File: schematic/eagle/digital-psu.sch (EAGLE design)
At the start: 79 parts, among them IC1 TL072P, IC2 TLC272P, Q1 MPSA56-TO92, T3 2N3055, T4 2N3055, T5 2N3055, X1 Vout, X2 PASS_TRANSISTORS, X3 AC_IN

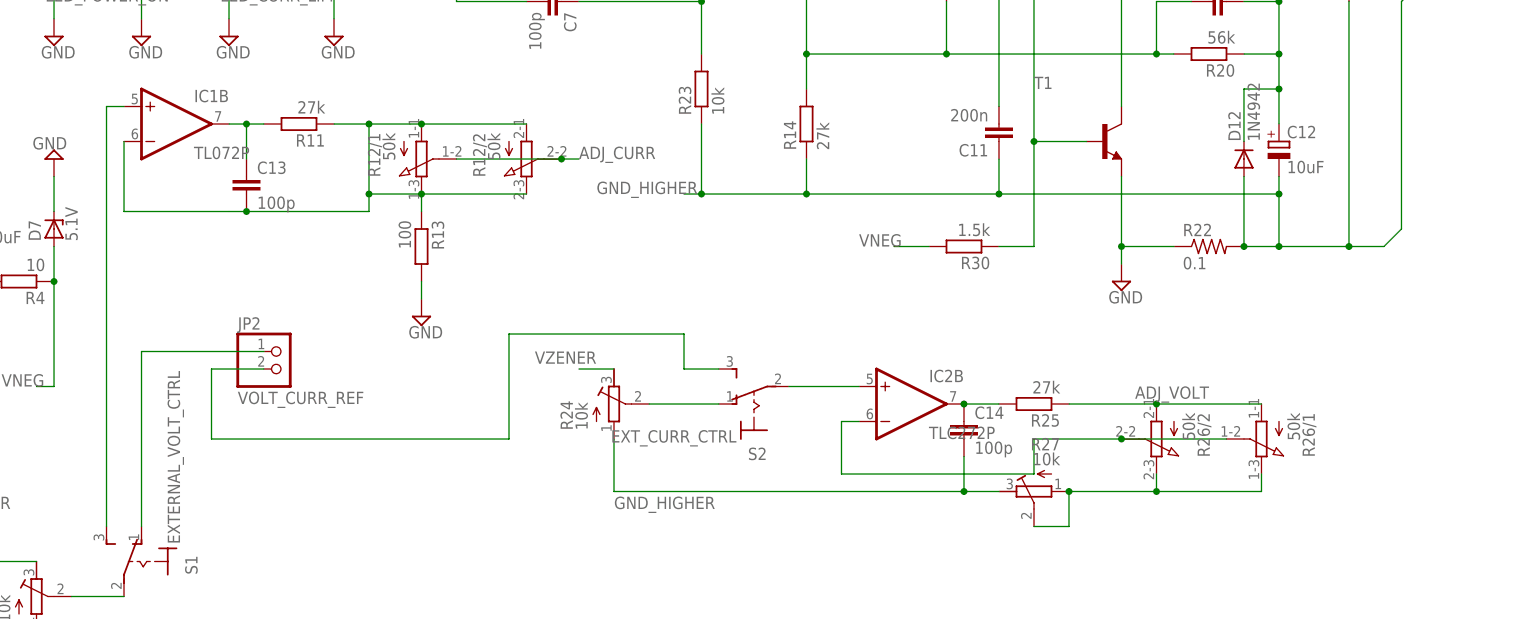
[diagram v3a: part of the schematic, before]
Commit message: op amp 27k protection fixed
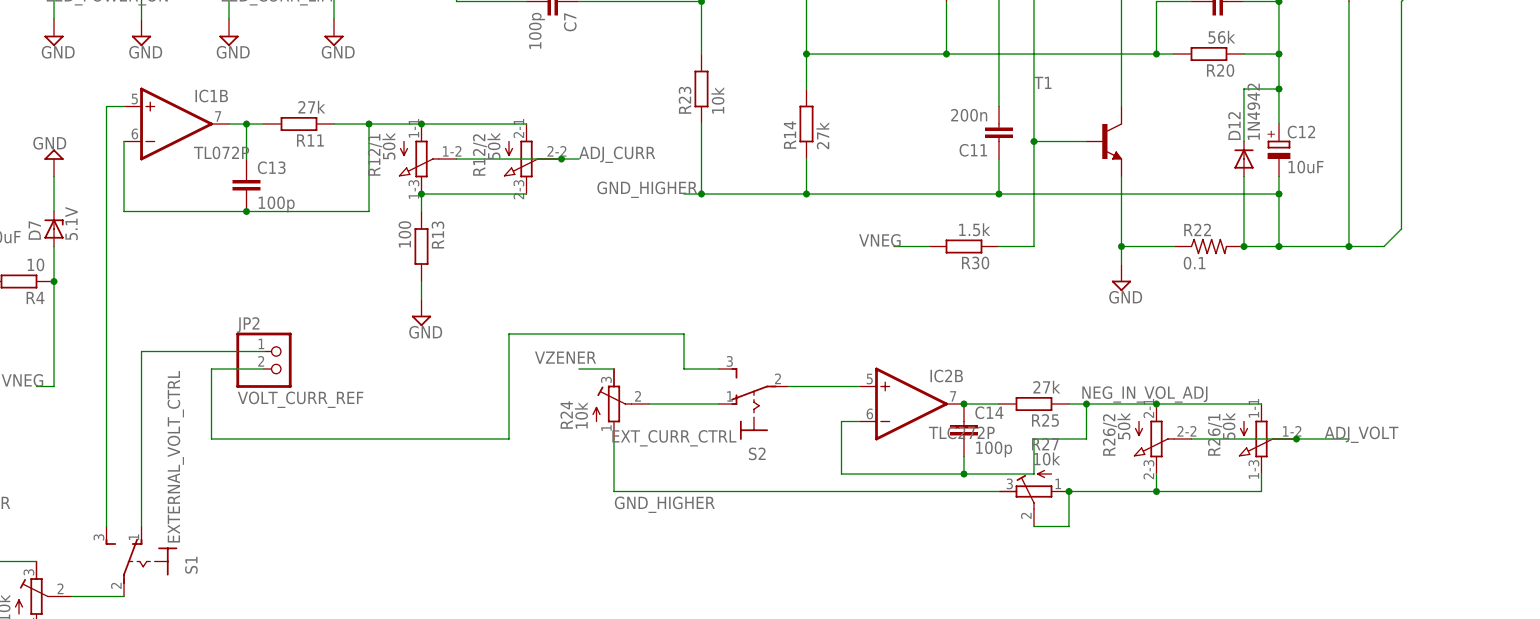
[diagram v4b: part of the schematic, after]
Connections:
- new net NEG_IN_VOL_ADJ: C14.2, IC2B.-IN, R25.1, R26/1.A, R26/2.A
- net ADJ_VOLT: now also R26/1.S, R26/2.S; no longer R25.1, R26/1.A, R26/2.A
- net GND_HIGHER: no longer C14.2
- net N$2: now also R12/1.E, R12/2.E, R13.1; no longer IC2B.-IN, R26/1.S, R26/2.S
- net N$20: no longer R12/1.E, R12/2.E, R13.1
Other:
- moved on the sheet: R26/1, R26/2
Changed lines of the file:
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@@
 <instance part="R17" gate="G$1" x="325.12" y="309.88"/>
 <instance part="R18" gate="G$1" x="320.04" y="299.72"/>
-<instance part="R26" gate="/1" x="320.04" y="208.28" rot="R180"/>
-<instance part="R26" gate="/2" x="304.8" y="208.28" rot="R180"/>
+<instance part="R26" gate="/1" x="320.04" y="208.28" rot="MR180"/>
+<instance part="R26" gate="/2" x="304.8" y="208.28" rot="MR180"/>
 <instance part="S1" gate="1" x="157.48" y="190.5" rot="MR0"/>
 <instance part="S2" gate="1" x="246.38" y="213.36" rot="R90"/>
@@
 <pinref part="R11" gate="G$1" pin="1"/>
 <wire x1="172.72" y1="241.3" x2="190.5" y2="241.3" width="0.1524" layer="91"/>
-<wire x1="190.5" y1="243.84" x2="190.5" y2="254" width="0.1524" layer="91"/>
+<wire x1="190.5" y1="241.3" x2="190.5" y2="254" width="0.1524" layer="91"/>
 <wire x1="190.5" y1="254" x2="185.42" y2="254" width="0.1524" layer="91"/>
 <pinref part="C13" gate="G$1" pin="2"/>
@@
 <junction x="198.12" y="254"/>
 <junction x="190.5" y="254"/>
-<wire x1="190.5" y1="241.3" x2="190.5" y2="243.84" width="0.1524" layer="91"/>
-<pinref part="R12" gate="/1" pin="E"/>
-<pinref part="R12" gate="/2" pin="E"/>
-<wire x1="213.36" y1="243.84" x2="198.12" y2="243.84" width="0.1524" layer="91"/>
-<pinref part="R13" gate="G$1" pin="1"/>
-<wire x1="198.12" y1="241.3" x2="198.12" y2="243.84" width="0.1524" layer="91"/>
-<junction x="198.12" y="243.84"/>
-<wire x1="190.5" y1="243.84" x2="198.12" y2="243.84" width="0.1524" layer="91"/>
-<junction x="190.5" y="243.84"/>
 <pinref part="IC1" gate="B" pin="-IN"/>
 <wire x1="154.94" y1="251.46" x2="154.94" y2="241.3" width="0.1524" layer="91"/>
-<wire x1="154.94" y1="241.3" x2="170.18" y2="241.3" width="0.1524" layer="91"/>
-<wire x1="170.18" y1="241.3" x2="172.72" y2="241.3" width="0.1524" layer="91"/>
+<wire x1="154.94" y1="241.3" x2="172.72" y2="241.3" width="0.1524" layer="91"/>
 <junction x="172.72" y="241.3"/>
 </segment>
@@
 <wire x1="226.06" y1="208.28" x2="226.06" y2="200.66" width="0.1524" layer="91"/>
 <label x="226.06" y="198.12" size="1.778" layer="95"/>
-<pinref part="C14" gate="G$1" pin="2"/>
-<wire x1="276.86" y1="205.74" x2="276.86" y2="200.66" width="0.1524" layer="91"/>
 <pinref part="R27" gate="G$1" pin="E"/>
-<wire x1="276.86" y1="200.66" x2="281.94" y2="200.66" width="0.1524" layer="91"/>
-<wire x1="276.86" y1="200.66" x2="226.06" y2="200.66" width="0.1524" layer="91"/>
-<junction x="276.86" y="200.66"/>
+<wire x1="281.94" y1="200.66" x2="226.06" y2="200.66" width="0.1524" layer="91"/>
 </segment>
 <segment>
@@
 <net name="ADJ_VOLT" class="0">
 <segment>
-<pinref part="R25" gate="G$1" pin="1"/>
-<pinref part="R26" gate="/2" pin="A"/>
-<wire x1="292.1" y1="213.36" x2="304.8" y2="213.36" width="0.1524" layer="91"/>
-<pinref part="R26" gate="/1" pin="A"/>
-<wire x1="304.8" y1="213.36" x2="320.04" y2="213.36" width="0.1524" layer="91"/>
-<junction x="304.8" y="213.36"/>
-<label x="312.42" y="215.9" size="1.778" layer="95" rot="R180"/>
-</segment>
-<segment>
 <wire x1="256.54" y1="287.02" x2="254" y2="287.02" width="0.1524" layer="91"/>
 <wire x1="254" y1="287.02" x2="254" y2="307.34" width="0.1524" layer="91"/>
@@
 <label x="259.08" y="309.88" size="1.778" layer="95" rot="R180"/>
 </segment>
-</net>
-<net name="N$2" class="0">
-<segment>
+<segment>
+<pinref part="R26" gate="/2" pin="S"/>
 <pinref part="R26" gate="/1" pin="S"/>
-<pinref part="R26" gate="/2" pin="S"/>
-<wire x1="314.96" y1="208.28" x2="299.72" y2="208.28" width="0.1524" layer="91"/>
-<wire x1="299.72" y1="208.28" x2="287.02" y2="208.28" width="0.1524" layer="91"/>
-<junction x="299.72" y="208.28"/>
-<wire x1="287.02" y1="208.28" x2="287.02" y2="203.2" width="0.1524" layer="91"/>
-<pinref part="IC2" gate="B" pin="-IN"/>
-<wire x1="261.62" y1="210.82" x2="259.08" y2="210.82" width="0.1524" layer="91"/>
-<wire x1="259.08" y1="210.82" x2="259.08" y2="203.2" width="0.1524" layer="91"/>
-<wire x1="287.02" y1="203.2" x2="259.08" y2="203.2" width="0.1524" layer="91"/>
+<wire x1="309.88" y1="208.28" x2="325.12" y2="208.28" width="0.1524" layer="91"/>
+<wire x1="325.12" y1="208.28" x2="332.74" y2="208.28" width="0.1524" layer="91"/>
+<junction x="325.12" y="208.28"/>
+<label x="329.184" y="208.28" size="1.778" layer="95"/>
 </segment>
 </net>
@@
 </segment>
 </net>
+<net name="NEG_IN_VOL_ADJ" class="0">
+<segment>
+<pinref part="R25" gate="G$1" pin="1"/>
+<pinref part="R26" gate="/2" pin="A"/>
+<wire x1="292.1" y1="213.36" x2="294.64" y2="213.36" width="0.1524" layer="91"/>
+<pinref part="R26" gate="/1" pin="A"/>
+<wire x1="294.64" y1="213.36" x2="304.8" y2="213.36" width="0.1524" layer="91"/>
+<wire x1="304.8" y1="213.36" x2="320.04" y2="213.36" width="0.1524" layer="91"/>
+<junction x="304.8" y="213.36"/>
+<label x="312.42" y="215.9" size="1.778" layer="95" rot="R180"/>
+<pinref part="IC2" gate="B" pin="-IN"/>
+<wire x1="261.62" y1="210.82" x2="259.08" y2="210.82" width="0.1524" layer="91"/>
+<wire x1="259.08" y1="210.82" x2="259.08" y2="203.2" width="0.1524" layer="91"/>
+<wire x1="294.64" y1="208.28" x2="287.02" y2="208.28" width="0.1524" layer="91"/>
+<wire x1="287.02" y1="208.28" x2="287.02" y2="203.2" width="0.1524" layer="91"/>
+<wire x1="259.08" y1="203.2" x2="276.86" y2="203.2" width="0.1524" layer="91"/>
+<pinref part="C14" gate="G$1" pin="2"/>
+<wire x1="276.86" y1="203.2" x2="287.02" y2="203.2" width="0.1524" layer="91"/>
+<wire x1="276.86" y1="203.2" x2="276.86" y2="205.74" width="0.1524" layer="91"/>
+<junction x="276.86" y="203.2"/>
+<wire x1="294.64" y1="208.28" x2="294.64" y2="213.36" width="0.1524" layer="91"/>
+<junction x="294.64" y="213.36"/>
+</segment>
+</net>
+<net name="N$2" class="0">
+<segment>
+<pinref part="R12" gate="/1" pin="E"/>
+<pinref part="R12" gate="/2" pin="E"/>
+<wire x1="213.36" y1="243.84" x2="198.12" y2="243.84" width="0.1524" layer="91"/>
+<junction x="198.12" y="243.84"/>
+<pinref part="R13" gate="G$1" pin="1"/>
+<wire x1="198.12" y1="241.3" x2="198.12" y2="243.84" width="0.1524" layer="91"/>
+</segment>
+</net>

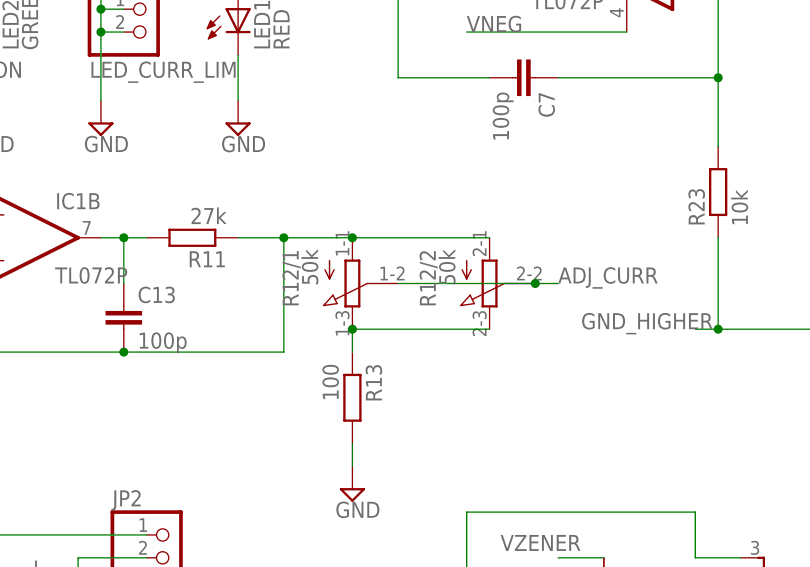
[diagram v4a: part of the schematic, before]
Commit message: added .spice files. In process of joining the two separate grounds
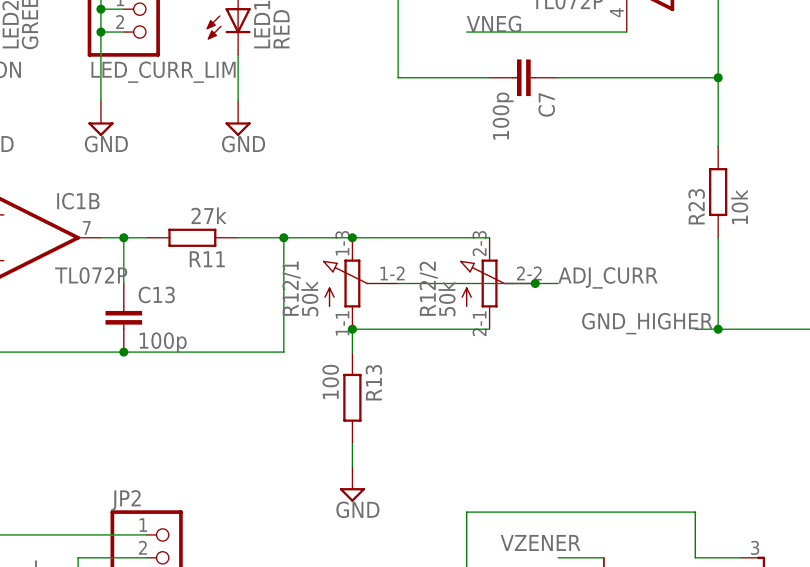
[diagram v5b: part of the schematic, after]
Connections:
- removed net N$2: R12/1.E, R12/2.E, R13.1
- new net N$32: R12/1.A, R12/2.A, R13.1
- net N$20: now also R12/1.E, R12/2.E; no longer R12/1.A, R12/2.A
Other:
- moved on the sheet: R12/1, R12/2
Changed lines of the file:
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@@
 <instance part="SUPPLY11" gate="GND" x="198.12" y="226.06"/>
 <instance part="IC1" gate="P" x="228.6" y="284.48"/>
-<instance part="R12" gate="/1" x="198.12" y="248.92" rot="MR180"/>
-<instance part="R12" gate="/2" x="213.36" y="248.92" rot="MR180"/>
+<instance part="R12" gate="/1" x="198.12" y="248.92"/>
+<instance part="R12" gate="/2" x="213.36" y="248.92"/>
 <instance part="D10" gate="1" x="241.3" y="307.34" rot="R180"/>
 <instance part="R14" gate="G$1" x="254" y="254" rot="R90"/>
@@
 <net name="N$20" class="0">
 <segment>
-<pinref part="R12" gate="/1" pin="A"/>
-<pinref part="R12" gate="/2" pin="A"/>
-<wire x1="213.36" y1="254" x2="198.12" y2="254" width="0.1524" layer="91"/>
 <pinref part="R11" gate="G$1" pin="1"/>
 <wire x1="172.72" y1="241.3" x2="190.5" y2="241.3" width="0.1524" layer="91"/>
@@
 <wire x1="190.5" y1="254" x2="185.42" y2="254" width="0.1524" layer="91"/>
 <pinref part="C13" gate="G$1" pin="2"/>
-<wire x1="198.12" y1="254" x2="190.5" y2="254" width="0.1524" layer="91"/>
-<junction x="198.12" y="254"/>
-<junction x="190.5" y="254"/>
 <pinref part="IC1" gate="B" pin="-IN"/>
 <wire x1="154.94" y1="251.46" x2="154.94" y2="241.3" width="0.1524" layer="91"/>
 <wire x1="154.94" y1="241.3" x2="172.72" y2="241.3" width="0.1524" layer="91"/>
 <junction x="172.72" y="241.3"/>
+<pinref part="R12" gate="/1" pin="E"/>
+<wire x1="190.5" y1="254" x2="198.12" y2="254" width="0.1524" layer="91"/>
+<junction x="190.5" y="254"/>
+<pinref part="R12" gate="/2" pin="E"/>
+<wire x1="198.12" y1="254" x2="213.36" y2="254" width="0.1524" layer="91"/>
+<junction x="198.12" y="254"/>
 </segment>
 </net>
@@
 <label x="220.98" y="248.92" size="1.778" layer="95"/>
 <pinref part="R12" gate="/2" pin="S"/>
+<wire x1="218.44" y1="248.92" x2="220.98" y2="248.92" width="0.1524" layer="91"/>
 <pinref part="R12" gate="/1" pin="S"/>
-<wire x1="203.2" y1="248.92" x2="218.44" y2="248.92" width="0.1524" layer="91"/>
+<wire x1="218.44" y1="248.92" x2="203.2" y2="248.92" width="0.1524" layer="91"/>
 <junction x="218.44" y="248.92"/>
-<wire x1="218.44" y1="248.92" x2="220.98" y2="248.92" width="0.1524" layer="91"/>
 </segment>
 <segment>
@@
 </segment>
 </net>
-<net name="N$2" class="0">
-<segment>
-<pinref part="R12" gate="/1" pin="E"/>
-<pinref part="R12" gate="/2" pin="E"/>
+<net name="N$32" class="0">
+<segment>
+<pinref part="R12" gate="/1" pin="A"/>
+<pinref part="R13" gate="G$1" pin="1"/>
+<wire x1="198.12" y1="241.3" x2="198.12" y2="243.84" width="0.1524" layer="91"/>
+<pinref part="R12" gate="/2" pin="A"/>
 <wire x1="213.36" y1="243.84" x2="198.12" y2="243.84" width="0.1524" layer="91"/>
 <junction x="198.12" y="243.84"/>
-<pinref part="R13" gate="G$1" pin="1"/>
-<wire x1="198.12" y1="241.3" x2="198.12" y2="243.84" width="0.1524" layer="91"/>
-</segment>
-</net>
+</segment>
+</net>
